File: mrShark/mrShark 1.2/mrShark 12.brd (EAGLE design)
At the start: 26 x 31 mm, 78 parts, among them IC1 ATMEGA168-20MU, IC2 PCA9540BDP, IC3 TIR1000PWR, IC4 TFBS4711TR1, IC5 DRV8830DRCT, IC6 LTC2990IMS#PBF, IC7 DRV8830DRCT, IC8 LTC2990IMS#PBF, Q1 TXC - 7X-1.8432MBB-T - OSC, 1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, Q2 BC817W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

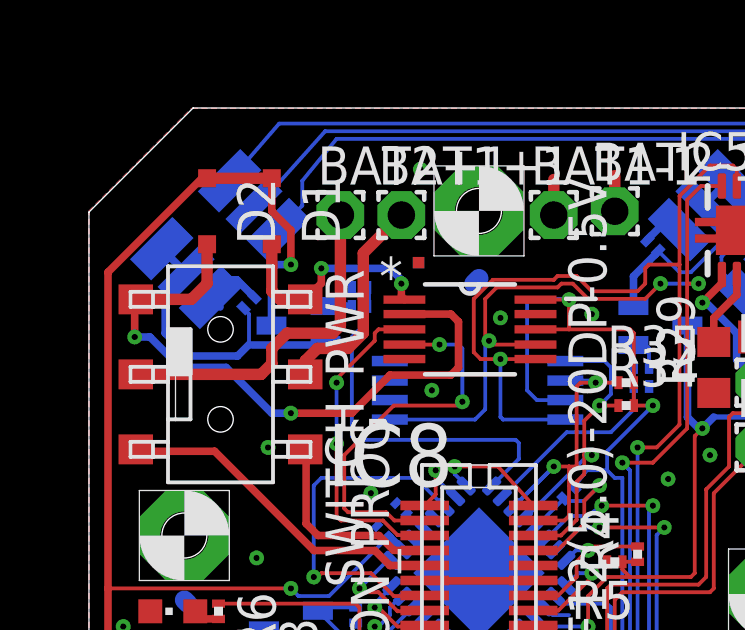
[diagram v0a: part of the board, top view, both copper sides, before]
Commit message: Updated mrShark 1.2 & 1.3 Updated mrShark Adapter Updated mrShark LED-Marker to version 0.0.3
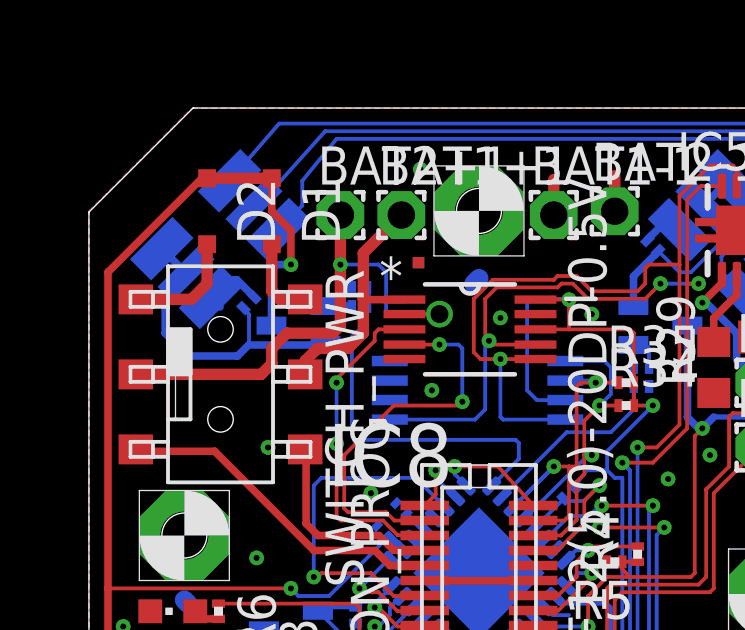
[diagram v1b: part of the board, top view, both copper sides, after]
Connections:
- net BAT1: now also IC8.1
- net BAT1+: no longer IC8.1
- net BAT2: now also IC8.2
- net BAT2+: no longer IC8.2
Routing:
- net BAT2+: track 21.1 -> 3.91 mm, vias 2 -> 0
- net BAT2: track 11.5 -> 17.4 mm, vias 0 -> 2
- net BAT1+: track 7.57 -> 2.79 mm, vias 2 -> 0
- net BAT1: track 7.26 -> 8.76 mm
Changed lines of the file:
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@@
 <?xml version="1.0" encoding="utf-8"?>
 <!DOCTYPE eagle SYSTEM "eagle.dtd">
-<eagle version="6.4">
+<eagle version="6.3">
 <drawing>
 <settings>
@@
 </signal>
 <signal name="BAT1+">
-<contactref element="IC8" pad="1"/>
 <contactref element="SWITCH_PWR" pad="1"/>
 <contactref element="D1" pad="A"/>
@@
 <wire x1="6.366" y1="24.622" x2="6.096" y2="24.892" width="0.381" layer="1"/>
 <wire x1="6.096" y1="24.892" x2="6.096" y2="26.459" width="0.381" layer="1"/>
-<wire x1="10.5156" y1="24.6126" x2="10.414" y2="24.7142" width="0.254" layer="1"/>
-<wire x1="10.414" y1="24.7142" x2="10.414" y2="25.146" width="0.254" layer="1"/>
-<via x="10.414" y="25.146" extent="1-16" drill="0.2" diameter="0.5" shape="octagon"/>
-<wire x1="10.414" y1="25.146" x2="10.414" y2="25.273" width="0.254" layer="16"/>
-<wire x1="10.414" y1="25.273" x2="10.033" y2="25.654" width="0.254" layer="16"/>
-<wire x1="10.033" y1="25.654" x2="7.747" y2="25.654" width="0.254" layer="16"/>
-<via x="7.747" y="25.654" extent="1-16" drill="0.2" diameter="0.5" shape="octagon"/>
-<wire x1="7.747" y1="25.654" x2="7.747" y2="25.159" width="0.254" layer="1"/>
-<wire x1="7.747" y1="25.159" x2="7.21" y2="24.622" width="0.254" layer="1"/>
 </signal>
 <signal name="BAT2+">
-<contactref element="IC8" pad="2"/>
 <contactref element="SWITCH_PWR" pad="4"/>
 <contactref element="D2" pad="A"/>
@@
 <wire x1="3.413" y1="24.622" x2="3.937" y2="25.146" width="0.381" layer="1"/>
 <wire x1="3.937" y1="25.146" x2="3.937" y2="26.459" width="0.381" layer="1"/>
-<wire x1="10.5156" y1="24.13" x2="12.065" y2="24.13" width="0.254" layer="1"/>
-<wire x1="12.065" y1="24.13" x2="12.319" y2="23.876" width="0.254" layer="1"/>
-<wire x1="12.319" y1="23.876" x2="12.319" y2="22.352" width="0.254" layer="1"/>
-<wire x1="12.319" y1="22.352" x2="12.065" y2="22.098" width="0.254" layer="1"/>
-<wire x1="12.065" y1="22.098" x2="10.033" y2="22.098" width="0.254" layer="1"/>
-<wire x1="10.033" y1="22.098" x2="8.763" y2="20.828" width="0.254" layer="1"/>
-<wire x1="8.763" y1="20.828" x2="6.731" y2="20.828" width="0.254" layer="1"/>
-<via x="6.731" y="20.828" extent="1-16" drill="0.2" diameter="0.5" shape="octagon"/>
-<wire x1="6.731" y1="20.828" x2="6.096" y2="20.828" width="0.254" layer="16"/>
-<wire x1="6.096" y1="20.828" x2="4.572" y2="22.352" width="0.254" layer="16"/>
-<wire x1="4.572" y1="22.352" x2="3.048" y2="22.352" width="0.254" layer="16"/>
-<wire x1="3.048" y1="22.352" x2="2.032" y2="23.368" width="0.254" layer="16"/>
-<wire x1="2.032" y1="23.368" x2="1.524" y2="23.368" width="0.254" layer="16"/>
-<via x="1.524" y="23.368" extent="1-16" drill="0.2" diameter="0.5" shape="octagon"/>
-<wire x1="1.524" y1="23.368" x2="1.524" y2="24.638" width="0.254" layer="1"/>
-<wire x1="1.524" y1="24.638" x2="1.56" y2="24.622" width="0" layer="19" extent="1-1"/>
 </signal>
 <signal name="N$28">
@@
 <wire x1="8.636" y1="22.987" x2="9.144" y2="23.495" width="0.381" layer="1"/>
 <wire x1="9.144" y1="23.495" x2="9.144" y2="24.638" width="0.381" layer="1"/>
-<wire x1="9.144" y1="24.638" x2="9.144" y2="26.162" width="0.381" layer="1"/>
+<wire x1="9.144" y1="24.638" x2="9.144" y2="24.765" width="0.381" layer="1"/>
+<wire x1="9.144" y1="24.765" x2="9.144" y2="26.162" width="0.381" layer="1"/>
 <wire x1="9.144" y1="26.162" x2="10.414" y2="27.432" width="0.381" layer="1"/>
 <wire x1="9.144" y1="24.6126" x2="9.144" y2="24.638" width="0.254" layer="1"/>
+<contactref element="IC8" pad="1"/>
+<wire x1="10.5156" y1="24.6126" x2="9.144" y2="24.6126" width="0.254" layer="1"/>
+<wire x1="9.144" y1="24.638" x2="9.144" y2="24.765" width="0.254" layer="1"/>
 </signal>
 <signal name="BAT2">
@@
 <wire x1="6.096" y1="22.987" x2="6.096" y2="22.479" width="0.381" layer="1"/>
 <wire x1="6.096" y1="22.479" x2="5.739" y2="22.122" width="0.381" layer="1"/>
-<wire x1="8.382" y1="23.749" x2="8.382" y2="27.432" width="0.381" layer="1"/>
+<wire x1="8.382" y1="23.749" x2="8.382" y2="25.781" width="0.381" layer="1"/>
+<contactref element="IC8" pad="2"/>
+<wire x1="8.382" y1="25.781" x2="8.382" y2="27.432" width="0.381" layer="1"/>
+<wire x1="10.5156" y1="24.13" x2="11.684" y2="24.13" width="0.127" layer="1"/>
+<via x="11.684" y="24.13" extent="1-16" drill="0.6" shape="square"/>
+<wire x1="11.684" y1="24.13" x2="10.033" y2="24.13" width="0.127" layer="16"/>
+<wire x1="10.033" y1="24.13" x2="9.906" y2="24.257" width="0.127" layer="16"/>
+<wire x1="9.906" y1="24.257" x2="9.906" y2="25.527" width="0.127" layer="16"/>
+<wire x1="9.906" y1="25.527" x2="9.652" y2="25.781" width="0.127" layer="16"/>
+<wire x1="9.652" y1="25.781" x2="8.382" y2="25.781" width="0.127" layer="16"/>
+<via x="8.382" y="25.781" extent="1-16" drill="0.2" diameter="0.5" shape="octagon"/>
 </signal>
 </signals>
